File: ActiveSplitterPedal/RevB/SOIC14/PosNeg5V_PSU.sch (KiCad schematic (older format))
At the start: 5 parts, among them U9 SE8250X2

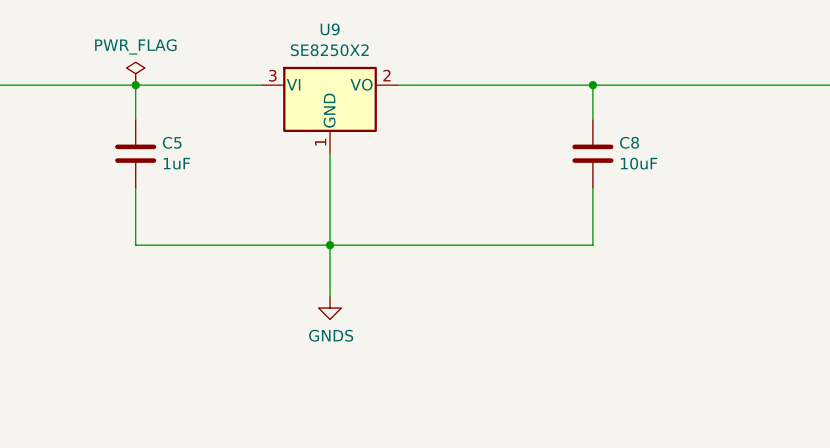
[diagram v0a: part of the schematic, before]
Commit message: updated hw
- Updated RevA charge pump RC post  filter component values for Fc=72KHz
- Updated RevA for gain opamp components
- Branched off RevB to improve design to use internal gain for peak detector
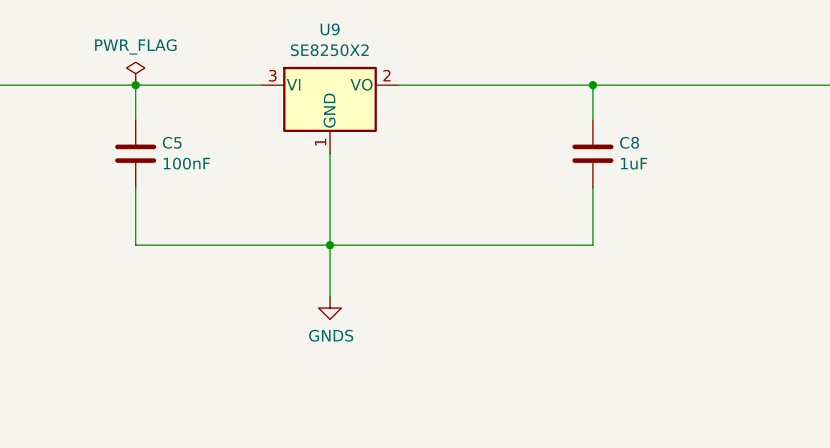
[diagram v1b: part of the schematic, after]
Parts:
- C10: value 1uF -> 100nF
- C12: value 10uF -> 1uF
- D5: footprint Diode_SMD:D_SMB_Handsoldering -> Diode_SMD:D_SOD-123F
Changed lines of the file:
@@
 F 0 "D5" H 5025 1459 50  0000 C CNN
 F 1 "B0520LW-RH" H 5025 1550 50  0000 C CNN
-F 2 "Diode_SMD:D_SMB_Handsoldering" H 5025 1675 50  0001 C CNN
+F 2 "Diode_SMD:D_SOD-123F" H 5025 1675 50  0001 C CNN
 F 3 "https://www.taiwansemi.com/products/datasheet/B0520LW%20SERIES_I1601.pdf" H 5025 1675 50  0001 C CNN
 	1    5025 1675
@@
 AR Path="/5F3902BC/5F1633CE" Ref="C5"  Part="1"
 F 0 "C5" H 6915 2021 50  0000 L CNN
-F 1 "1uF" H 6915 1930 50  0000 L CNN
+F 1 "100nF" H 6915 1930 50  0000 L CNN
 F 2 "Capacitor_SMD:C_0805_2012Metric_Pad1.15x1.40mm_HandSolder" H 6838 1825 50  0001 C CNN
 F 3 "~" H 6800 1975 50  0001 C CNN
@@
 AR Path="/5F3902BC/5F16440D" Ref="C8"  Part="1"
 F 0 "C8" H 8915 2021 50  0000 L CNN
-F 1 "10uF" H 8915 1930 50  0000 L CNN
+F 1 "1uF" H 8915 1930 50  0000 L CNN
 F 2 "Capacitor_SMD:C_0805_2012Metric_Pad1.15x1.40mm_HandSolder" H 8838 1825 50  0001 C CNN
 F 3 "~" H 8800 1975 50  0001 C CNN
